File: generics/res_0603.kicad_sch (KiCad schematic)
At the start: 9 parts

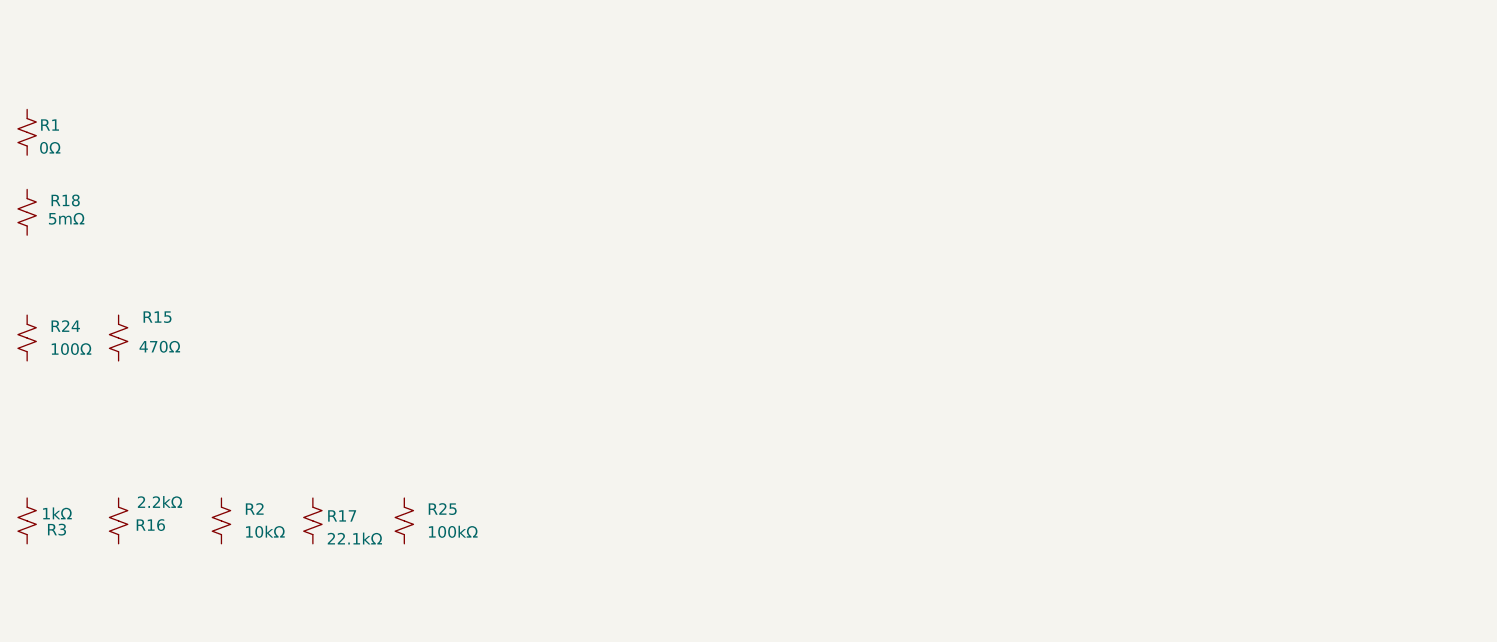
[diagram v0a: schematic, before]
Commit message: Add ESP32 and relevant peripherals
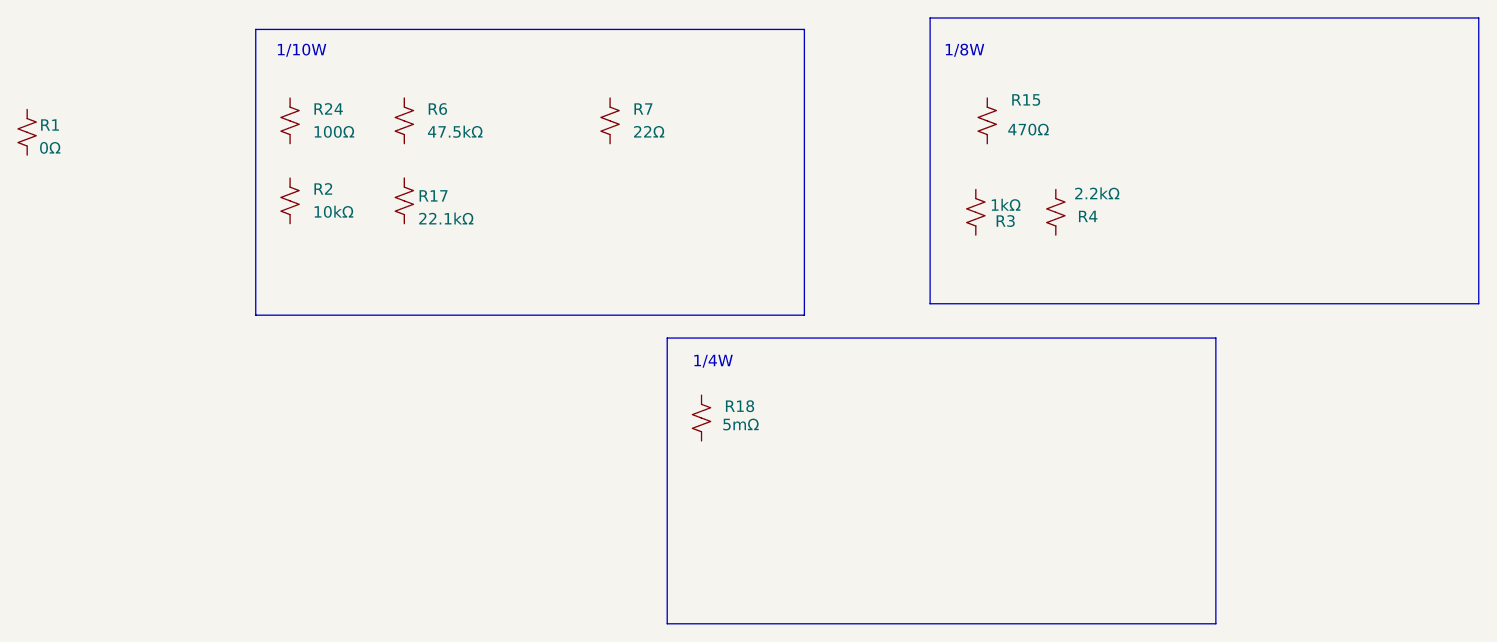
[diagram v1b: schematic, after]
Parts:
- removed R16: 2.2kΩ, Capacitor_SMD:C_0603_1608Metric, symbol Device:R_Small_US
- removed R25: 100kΩ, Resistor_SMD:R_0603_1608Metric, symbol Device:R_Small_US
- added R4: 2.2kΩ, Capacitor_SMD:C_0603_1608Metric, symbol Device:R_Small_US
- added R6: 47.5kΩ, Resistor_SMD:R_0603_1608Metric, symbol Device:R_Small_US
- added R7: 22Ω, Resistor_SMD:R_0603_1608Metric, symbol Device:R_Small_US
- R17: Pwr (none) -> 1/10W
- R18: Pwr (none) -> 1/4W
- R3: Mfr Vishay Dale -> Vishay; Pwr (none) -> 1/8W
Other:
- note added: "1/10W"
- note added: "1/4W"
- note added: "1/8W"
- moved on the sheet: R15, R17, R18, R2, R24, R3

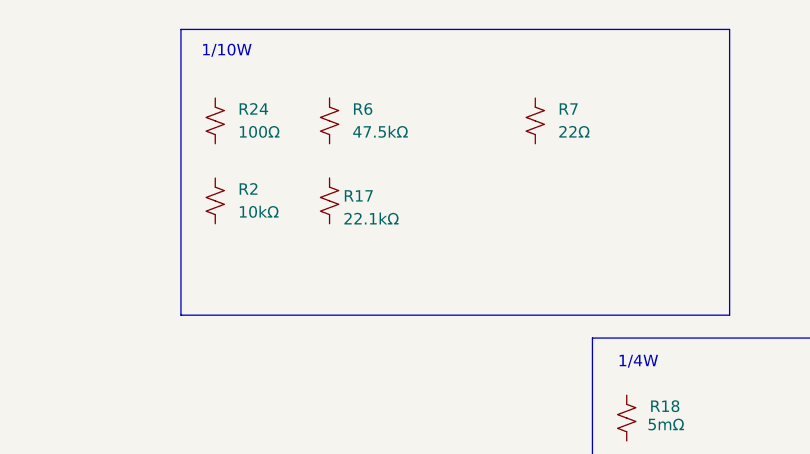
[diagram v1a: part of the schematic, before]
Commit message: - Generics updates - Add LED library
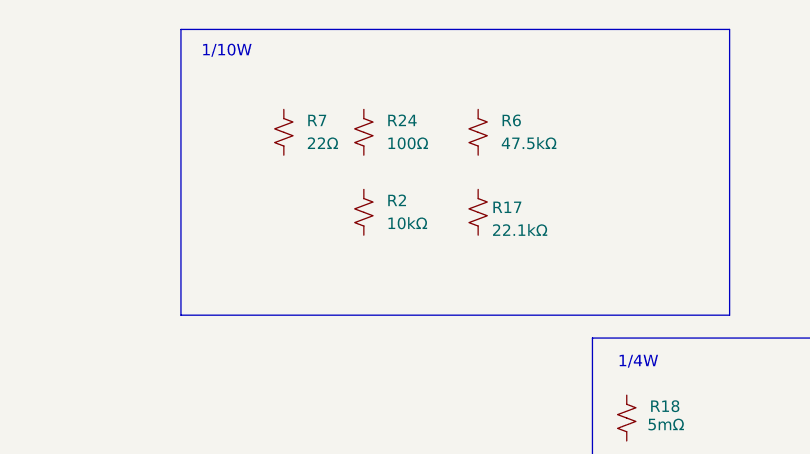
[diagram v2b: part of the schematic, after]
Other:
- moved on the sheet: R17, R2, R24, R6, R7
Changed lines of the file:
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@@
 	(symbol
 		(lib_id "Device:R_Small_US")
-		(at 60.96 36.83 0)
+		(at 77.47 38.1 0)
 		(unit 1)
 		(exclude_from_sim no)
@@
 		(fields_autoplaced yes)
 		(property "Reference" "R6"
-			(at 63.5 35.5599 0)
+			(at 80.01 36.8299 0)
 			(effects
 				(font
@@
 		)
 		(property "Value" "47.5kΩ"
-			(at 63.5 38.0999 0)
+			(at 80.01 39.3699 0)
 			(effects
 				(font
@@
 		)
 		(property "Footprint" "Resistor_SMD:R_0603_1608Metric"
-			(at 60.96 36.83 0)
+			(at 77.47 38.1 0)
 			(effects
 				(font
@@
 		)
 		(property "Datasheet" "~"
-			(at 60.96 36.83 0)
+			(at 77.47 38.1 0)
 			(effects
 				(font
@@
 		)
 		(property "Description" "Resistor, small US symbol"
-			(at 60.96 36.83 0)
+			(at 77.47 38.1 0)
 			(effects
 				(font
@@
 		)
 		(property "MPN" "MCT06030C4752FP500"
-			(at 60.96 36.83 0)
+			(at 77.47 38.1 0)
 			(effects
 				(font
@@
 		)
 		(property "Mfr" "Vishay"
-			(at 60.96 36.83 0)
+			(at 77.47 38.1 0)
 			(effects
 				(font
@@
 		)
 		(property "Power" "1/10W"
-			(at 60.96 36.83 0)
+			(at 77.47 38.1 0)
 			(effects
 				(font
@@
 		)
 		(property "Tolerance" "1%"
-			(at 60.96 36.83 0)
+			(at 77.47 38.1 0)
 			(effects
 				(font
@@
 	(symbol
 		(lib_id "Device:R_Small_US")
-		(at 48.26 36.83 180)
+		(at 64.77 38.1 180)
 		(unit 1)
 		(exclude_from_sim no)
@@
 		(fields_autoplaced yes)
 		(property "Reference" "R24"
-			(at 50.8 35.5599 0)
+			(at 67.31 36.8299 0)
 			(effects
 				(font
@@
 		)
 		(property "Value" "100Ω"
-			(at 50.8 38.0999 0)
+			(at 67.31 39.3699 0)
 			(effects
 				(font
@@
 		)
 		(property "Footprint" "Resistor_SMD:R_0603_1608Metric"
-			(at 48.26 36.83 0)
+			(at 64.77 38.1 0)
 			(effects
 				(font
@@
 		)
 		(property "Datasheet" "~"
-			(at 48.26 36.83 0)
+			(at 64.77 38.1 0)
 			(effects
 				(font
@@
 		)
 		(property "Description" "Resistor, small US symbol"
-			(at 48.26 36.83 0)
+			(at 64.77 38.1 0)
 			(effects
 				(font
@@
 		)
 		(property "MPN" "RC0603FR-07100RL"
-			(at 48.26 36.83 90)
+			(at 64.77 38.1 90)
 			(effects
 				(font
@@
 		)
 		(property "Mfr" "YAGEO"
-			(at 48.26 36.83 90)
+			(at 64.77 38.1 90)
 			(effects
 				(font
@@
 		)
 		(property "Tolerance" "1%"
-			(at 48.26 36.83 90)
+			(at 64.77 38.1 90)
 			(effects
 				(font
@@
 		)
 		(property "Power" "1/10W"
-			(at 48.26 36.83 90)
+			(at 64.77 38.1 90)
 			(effects
 				(font
@@
 	(symbol
 		(lib_id "Device:R_Small_US")
-		(at 60.96 45.72 0)
+		(at 77.47 46.99 0)
 		(unit 1)
 		(exclude_from_sim no)
@@
 		(dnp no)
 		(property "Reference" "R17"
-			(at 62.484 45.212 0)
+			(at 78.994 46.482 0)
 			(effects
 				(font
@@
 		)
 		(property "Value" "22.1kΩ"
-			(at 62.484 47.752 0)
+			(at 78.994 49.022 0)
 			(effects
 				(font
@@
 		)
 		(property "Footprint" "Resistor_SMD:R_0603_1608Metric"
-			(at 60.96 45.72 0)
+			(at 77.47 46.99 0)
 			(effects
 				(font
@@
 		)
 		(property "Datasheet" "~"
-			(at 60.96 45.72 0)
+			(at 77.47 46.99 0)
 			(effects
 				(font
@@
 		)
 		(property "Description" "Resistor, small US symbol"
-			(at 60.96 45.72 0)
+			(at 77.47 46.99 0)
 			(effects
 				(font
@@
 		)
 		(property "MPN" "RC0603FR-0722K1L"
-			(at 60.96 45.72 0)
+			(at 77.47 46.99 0)
 			(effects
 				(font
@@
 		)
 		(property "Mfr" "YAGEO"
-			(at 60.96 45.72 0)
+			(at 77.47 46.99 0)
 			(effects
 				(font
@@
 		)
 		(property "Pwr" "1/10W"
-			(at 60.96 45.72 0)
+			(at 77.47 46.99 0)
 			(effects
 				(font
@@
 	(symbol
 		(lib_id "Device:R_Small_US")
-		(at 83.82 36.83 0)
+		(at 55.88 38.1 0)
 		(unit 1)
 		(exclude_from_sim no)
@@
 		(fields_autoplaced yes)
 		(property "Reference" "R7"
-			(at 86.36 35.5599 0)
+			(at 58.42 36.8299 0)
 			(effects
 				(font
@@
 		)
 		(property "Value" "22Ω"
-			(at 86.36 38.0999 0)
+			(at 58.42 39.3699 0)
 			(effects
 				(font
@@
 		)
 		(property "Footprint" "Resistor_SMD:R_0603_1608Metric"
-			(at 83.82 36.83 0)
+			(at 55.88 38.1 0)
 			(effects
 				(font
@@
 		)
 		(property "Datasheet" "~"
-			(at 83.82 36.83 0)
+			(at 55.88 38.1 0)
 			(effects
 				(font
@@
 		)
 		(property "Description" "Resistor, small US symbol"
-			(at 83.82 36.83 0)
+			(at 55.88 38.1 0)
 			(effects
 				(font
@@
 		)
 		(property "MPN" "RC0603FR-0722RL"
-			(at 83.82 36.83 0)
+			(at 55.88 38.1 0)
 			(effects
 				(font
@@
 		)
 		(property "Mfr" "YAGEO"
-			(at 83.82 36.83 0)
+			(at 55.88 38.1 0)
 			(effects
 				(font
@@
 		)
 		(property "Power" "1/10W"
-			(at 83.82 36.83 0)
+			(at 55.88 38.1 0)
 			(effects
 				(font
@@
 		)
 		(property "Tolerance" "1%"
-			(at 83.82 36.83 0)
+			(at 55.88 38.1 0)
 			(effects
 				(font
@@
 	(symbol
 		(lib_id "Device:R_Small_US")
-		(at 48.26 45.72 0)
+		(at 64.77 46.99 0)
 		(unit 1)
 		(exclude_from_sim no)
@@
 		(fields_autoplaced yes)
 		(property "Reference" "R2"
-			(at 50.8 44.4499 0)
+			(at 67.31 45.7199 0)
 			(effects
 				(font
@@
 		)
 		(property "Value" "10kΩ"
-			(at 50.8 46.9899 0)
+			(at 67.31 48.2599 0)
 			(effects
 				(font
@@
 		)
 		(property "Footprint" "Resistor_SMD:R_0603_1608Metric"
-			(at 48.26 45.72 0)
+			(at 64.77 46.99 0)
 			(effects
 				(font
@@
 		)
 		(property "Datasheet" "~"
-			(at 48.26 45.72 0)
+			(at 64.77 46.99 0)
 			(effects
 				(font
@@
 		)
 		(property "Description" "Resistor, small US symbol"
-			(at 48.26 45.72 0)
+			(at 64.77 46.99 0)
 			(effects
 				(font
@@
 		)
 		(property "MPN" "RC0603FR-0710KL"
-			(at 48.26 45.72 0)
+			(at 64.77 46.99 0)
 			(effects
 				(font
@@
 		)
 		(property "Mfr" "YAGEO"
-			(at 48.26 45.72 0)
+			(at 64.77 46.99 0)
 			(effects
 				(font
@@
 		)
 		(property "Power" "1/10W"
-			(at 48.26 45.72 0)
+			(at 64.77 46.99 0)
 			(effects
 				(font
@@
 		)
 		(property "Tolerance" "1%"
-			(at 48.26 45.72 0)
-			(effects
-				(font
+			(at 64.77 46.99 0)
+			(effects
+				(font

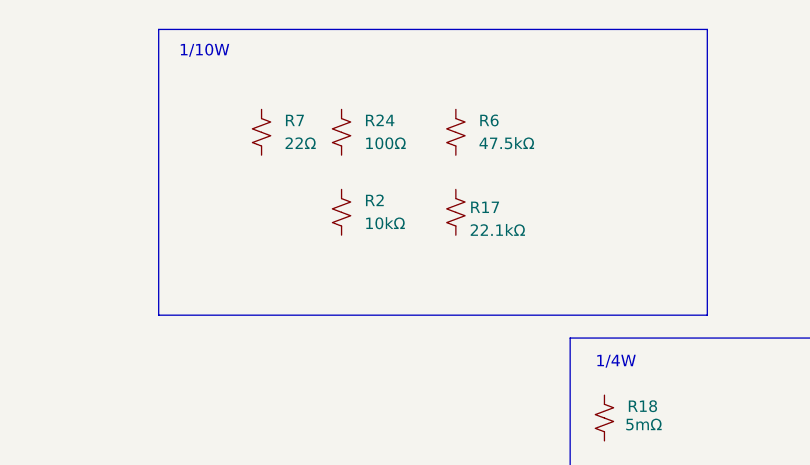
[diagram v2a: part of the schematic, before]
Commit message: Add parts for V0 status indicator light project
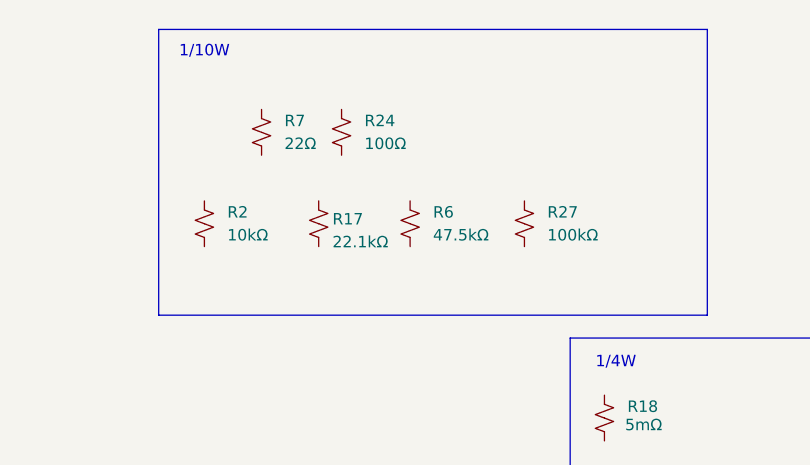
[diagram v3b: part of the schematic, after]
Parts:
- added R27: 100kΩ, Resistor_SMD:R_0603_1608Metric, symbol Device:R_Small_US
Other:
- moved on the sheet: R17, R2, R6
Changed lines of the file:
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@@
 	(symbol
 		(lib_id "Device:R_Small_US")
-		(at 77.47 38.1 0)
+		(at 72.39 48.26 0)
 		(unit 1)
 		(exclude_from_sim no)
@@
 		(fields_autoplaced yes)
 		(property "Reference" "R6"
-			(at 80.01 36.8299 0)
+			(at 74.93 46.9899 0)
 			(effects
 				(font
@@
 		)
 		(property "Value" "47.5kΩ"
-			(at 80.01 39.3699 0)
+			(at 74.93 49.5299 0)
 			(effects
 				(font
@@
 		)
 		(property "Footprint" "Resistor_SMD:R_0603_1608Metric"
-			(at 77.47 38.1 0)
+			(at 72.39 48.26 0)
 			(effects
 				(font
@@
 		)
 		(property "Datasheet" "~"
-			(at 77.47 38.1 0)
+			(at 72.39 48.26 0)
 			(effects
 				(font
@@
 		)
 		(property "Description" "Resistor, small US symbol"
-			(at 77.47 38.1 0)
+			(at 72.39 48.26 0)
 			(effects
 				(font
@@
 		)
 		(property "MPN" "MCT06030C4752FP500"
-			(at 77.47 38.1 0)
+			(at 72.39 48.26 0)
 			(effects
 				(font
@@
 		)
 		(property "Mfr" "Vishay"
-			(at 77.47 38.1 0)
+			(at 72.39 48.26 0)
 			(effects
 				(font
@@
 		)
 		(property "Power" "1/10W"
-			(at 77.47 38.1 0)
+			(at 72.39 48.26 0)
 			(effects
 				(font
@@
 		)
 		(property "Tolerance" "1%"
-			(at 77.47 38.1 0)
+			(at 72.39 48.26 0)
 			(effects
 				(font
@@
 	(symbol
 		(lib_id "Device:R_Small_US")
-		(at 77.47 46.99 0)
+		(at 62.23 48.26 0)
 		(unit 1)
 		(exclude_from_sim no)
@@
 		(dnp no)
 		(property "Reference" "R17"
-			(at 78.994 46.482 0)
+			(at 63.754 47.752 0)
 			(effects
 				(font
@@
 		)
 		(property "Value" "22.1kΩ"
-			(at 78.994 49.022 0)
+			(at 63.754 50.292 0)
 			(effects
 				(font
@@
 		)
 		(property "Footprint" "Resistor_SMD:R_0603_1608Metric"
-			(at 77.47 46.99 0)
+			(at 62.23 48.26 0)
 			(effects
 				(font
@@
 		)
 		(property "Datasheet" "~"
-			(at 77.47 46.99 0)
+			(at 62.23 48.26 0)
 			(effects
 				(font
@@
 		)
 		(property "Description" "Resistor, small US symbol"
-			(at 77.47 46.99 0)
+			(at 62.23 48.26 0)
 			(effects
 				(font
@@
 		)
 		(property "MPN" "RC0603FR-0722K1L"
-			(at 77.47 46.99 0)
+			(at 62.23 48.26 0)
 			(effects
 				(font
@@
 		)
 		(property "Mfr" "YAGEO"
-			(at 77.47 46.99 0)
+			(at 62.23 48.26 0)
 			(effects
 				(font
@@
 		)
 		(property "Pwr" "1/10W"
-			(at 77.47 46.99 0)
+			(at 62.23 48.26 0)
 			(effects
 				(font
@@
 	(symbol
 		(lib_id "Device:R_Small_US")
-		(at 64.77 46.99 0)
+		(at 49.53 48.26 0)
 		(unit 1)
 		(exclude_from_sim no)
@@
 		(fields_autoplaced yes)
 		(property "Reference" "R2"
-			(at 67.31 45.7199 0)
+			(at 52.07 46.9899 0)
 			(effects
 				(font
@@
 		)
 		(property "Value" "10kΩ"
-			(at 67.31 48.2599 0)
+			(at 52.07 49.5299 0)
 			(effects
 				(font
@@
 		)
 		(property "Footprint" "Resistor_SMD:R_0603_1608Metric"
-			(at 64.77 46.99 0)
+			(at 49.53 48.26 0)
 			(effects
 				(font
@@
 		)
 		(property "Datasheet" "~"
-			(at 64.77 46.99 0)
+			(at 49.53 48.26 0)
 			(effects
 				(font
@@
 		)
 		(property "Description" "Resistor, small US symbol"
-			(at 64.77 46.99 0)
+			(at 49.53 48.26 0)
 			(effects
 				(font
@@
 		)
 		(property "MPN" "RC0603FR-0710KL"
-			(at 64.77 46.99 0)
+			(at 49.53 48.26 0)
 			(effects
 				(font
@@
 		)
 		(property "Mfr" "YAGEO"
-			(at 64.77 46.99 0)
+			(at 49.53 48.26 0)
 			(effects
 				(font
@@
 		)
 		(property "Power" "1/10W"
-			(at 64.77 46.99 0)
+			(at 49.53 48.26 0)
 			(effects
 				(font
@@
 		)
 		(property "Tolerance" "1%"
-			(at 64.77 46.99 0)
+			(at 49.53 48.26 0)
 			(effects
 				(font
@@
 					(unit 1)
 				)
+			)
+		)
+	)
+	(symbol
+		(lib_id "Device:R_Small_US")
+		(at 85.09 48.26 0)
+		(unit 1)
+		(exclude_from_sim no)
+		(in_bom yes)
+		(on_board yes)
+		(dnp no)
+		(property "Reference" "R27"
+			(at 87.63 46.9899 0)
+			(effects
+				(font
+					(size 1.27 1.27)
+				)
+				(justify left)
+			)
+		)
+		(property "Value" "100kΩ"
+			(at 87.63 49.5299 0)
+			(effects
+				(font
+					(size 1.27 1.27)
+				)
+				(justify left)
+			)
+		)
+		(property "Footprint" "Resistor_SMD:R_0603_1608Metric"
+			(at 85.09 48.26 0)
+			(effects
+				(font
+					(size 1.27 1.27)
+				)
+				(hide yes)
+			)
+		)
+		(property "Datasheet" "~"
+			(at 85.09 48.26 0)
+			(effects
+				(font
+					(size 1.27 1.27)
+				)
+				(hide yes)
+			)
+		)
+		(property "Description" "Resistor, small US symbol"
+			(at 85.09 48.26 0)
+			(effects
+				(font
+					(size 1.27 1.27)
+				)
+				(hide yes)
+			)
+		)
+		(property "MPN" "RC0603FR-07100KL"
+			(at 85.09 48.26 0)
+			(effects
+				(font
+					(size 1.27 1.27)
+				)
+				(hide yes)
+			)
+		)
+		(property "Mfr" "YAGEO"
+			(at 85.09 48.26 0)
+			(effects
+				(font
+					(size 1.27 1.27)
+				)
+				(hide yes)
+			)
+		)
+		(property "Pwr" "1/10W"
+			(at 85.09 48.26 0)
+			(effects
+				(font
+					(size 1.27 1.27)
+				)
+				(hide yes)
+			)
+		)
+		(pin "2"
+		)
+		(pin "1"
+		)
+		(instances
+			(project "generics"
+				(path "/ff075d90-2677-48ca-91fd-a3a441ca4e63/a9c3687f-ffca-4c13-806c-b078a5c187c5"
+					(reference "R27")
+					(unit 1)
+				)
